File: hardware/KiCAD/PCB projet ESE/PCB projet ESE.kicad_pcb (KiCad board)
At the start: 4 copper layers, 57 x 54 mm, 95 parts, among them J1 Conn_01x06, J10 Conn_01x06, J11 Conn_01x06, J12 Conn_01x06, J13 Conn_01x06, J14 Conn_01x06, J15 Conn_01x06, J16 Conn_01x03, J2 Conn_01x04, J26 USB_C_Receptacle_USB2.0_16P, J3 Conn_01x06, J4 Conn_01x06, J5 Conn_01x04, J6 Conn_01x02, J7 Conn_ST_STDC14, J8 Conn_01x06, J9 Conn_01x06, SW1 SW_SPST, SW2 472121010111, U1 ZXBM5210-SP, U2 ZXBM5210-SP, U3 STM32G474RETx, U4 ADXL343, U5 USBLC6-2SC6

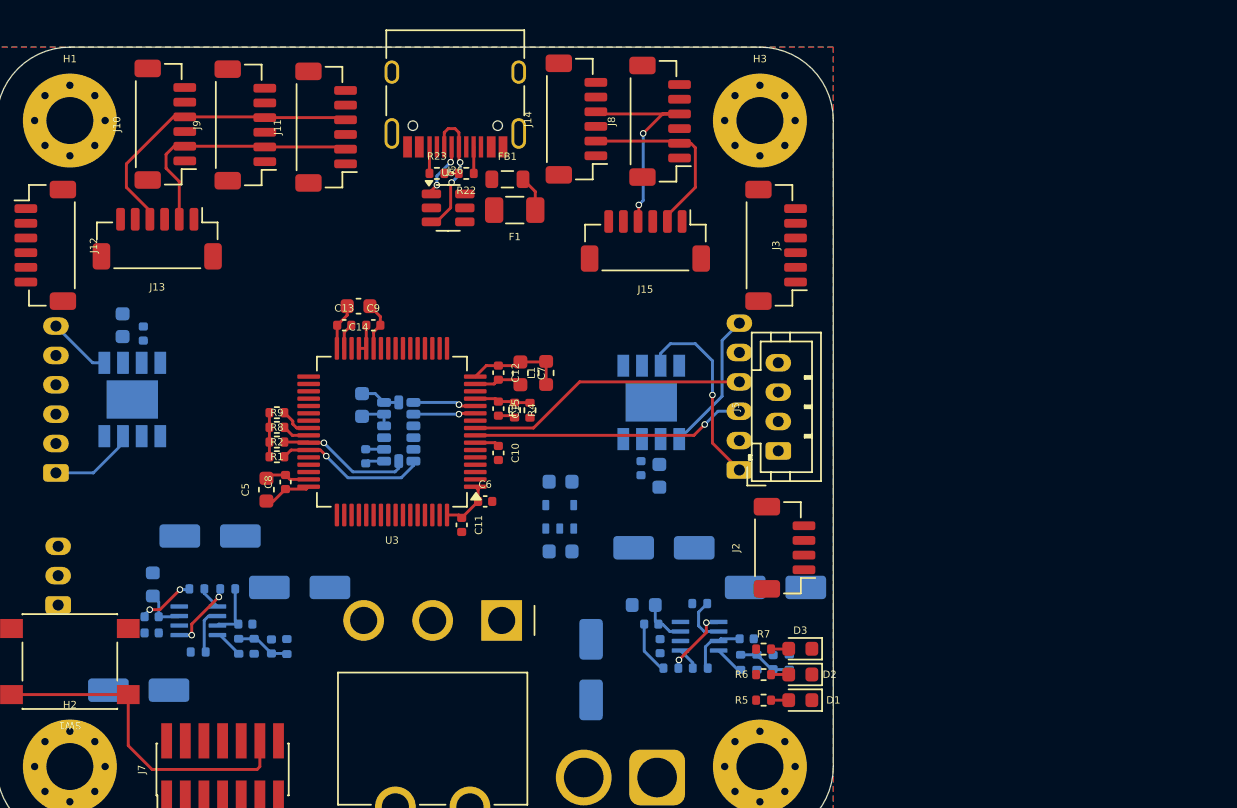
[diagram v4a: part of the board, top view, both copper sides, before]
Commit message: replace usb c by jst xh
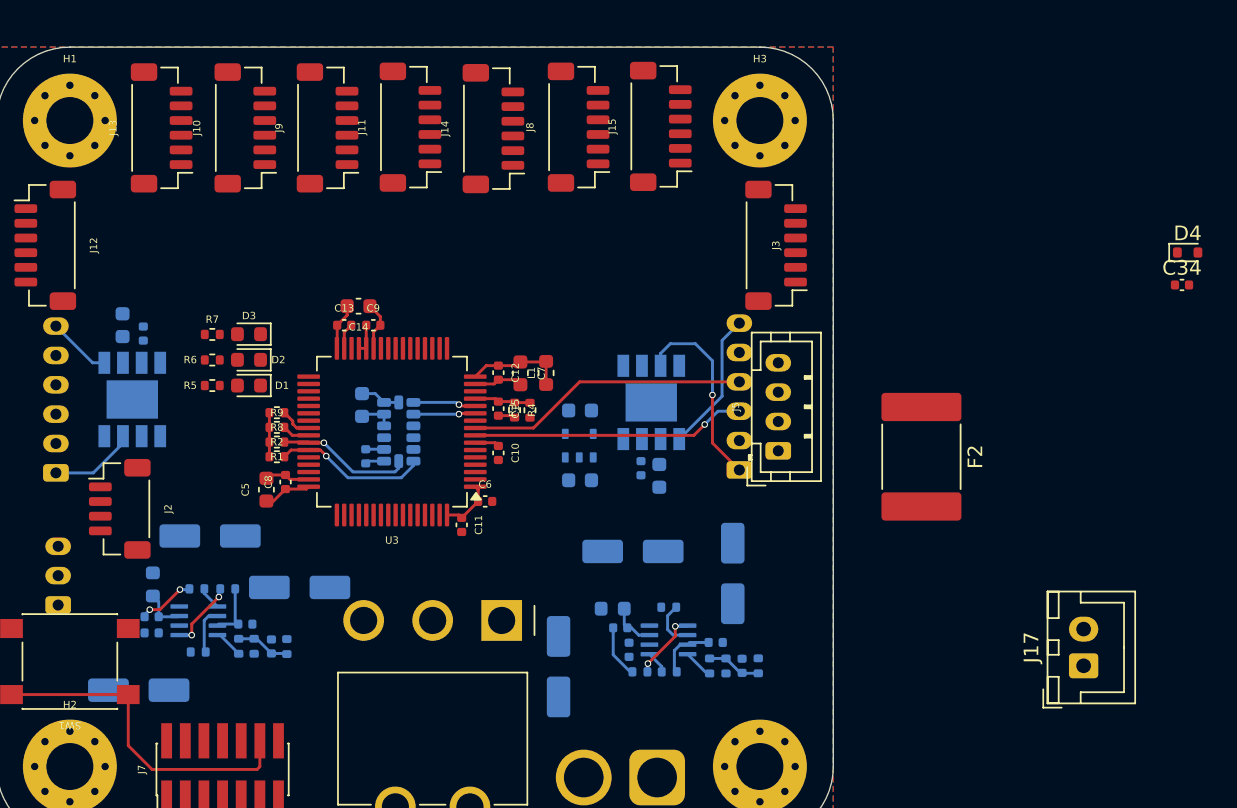
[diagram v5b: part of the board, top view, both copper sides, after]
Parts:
- removed F1: 250mA, Fuse:Fuse_1206_3216Metric
- removed FB1: 600 @ 100MHz, Inductor_SMD:L_0805_2012Metric
- removed J26: USB_C_Receptacle_USB2.0_16P, Connector_USB:USB_C_Receptacle_HRO_TYPE-C-31-M-12
- removed R22, R23: 5k1, Resistor_SMD:R_0402_1005Metric
- removed U5: USBLC6-2SC6, Package_TO_SOT_SMD:SOT-23-6
- added C34: 100n, Capacitor_SMD:C_0402_1005Metric, F.Cu at (159.8, 62.2)
- added D4: D_TVS_Small, Diode_SMD:D_SOD-523, F.Cu at (160.1, 60.0)
- added F2: 3.3A, Fuse:Fuse_2920_7451Metric, F.Cu at (142.0, 73.9)
- added J17: Conn_01x02, Connector_JST:JST_XH_B2B-XH-A_1x02_P2.50mm_Vertical, F.Cu at (153.1, 88.1)
- moved J2 45.4 mm to (87.4, 77.5), turned to -90 degrees
- moved D1 43.2 mm to (96.2, 69.0)
- moved D2 43.2 mm to (96.2, 67.3)
- moved D3 43.2 mm to (96.2, 65.5)
- moved R5 43.2 mm to (93.7, 69.0)
- moved R7 43.2 mm to (93.7, 65.6)
- moved R6 43.2 mm to (93.7, 67.3)
- moved J15 7.87 mm to (124.2, 51.4), turned to 90 degrees
- moved J13 7.56 mm to (90.2, 51.5), turned to 90 degrees
- moved J11 5.75 mm to (107.2, 51.5)
- moved J14 5.69 mm to (112.8, 51.5)
- moved J9 5.60 mm to (101.5, 51.5)
- moved J8 5.56 mm to (118.7, 51.5)
- moved J10 5.46 mm to (96.0, 51.5)
- moved BUxxSD1 5.03 mm to (118.7, 73.1)
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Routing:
- net SDA TOF: track 37.6 -> 1.88 mm, vias 2 -> 0
- net SCL TOF: track 32.3 -> 2.20 mm
- net D+: track 9.33 -> 0.00 mm, vias 2 -> 0
- net D-: track 3.77 -> 0.00 mm, vias 2 -> 0
- net Net-(F1-Pad1): track 2.45 -> 0.00 mm
- net Net-(J26-CC2): track 1.81 -> 0.00 mm
- net Net-(J26-CC1): track 1.81 -> 0.00 mm
- net Net-(D3-A): track 1.21 -> 0.00 mm
- net Net-(D2-A): track 1.21 -> 0.00 mm
- net Net-(D1-A): track 1.20 -> 0.00 mm
- net GND: track 17.3 -> 16.3 mm

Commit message: v1 PCB
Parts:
- removed C29, C30, C31: 22u, Capacitor_SMD:C_Elec_5x5.4
- removed C32, C33: 1u, Capacitor_SMD:C_0603_1608Metric
- removed C34: 100n, Capacitor_SMD:C_0402_1005Metric
- removed F2: 3.3A, Fuse:Fuse_2920_7451Metric
- removed J16: Conn_01x03, Connector_JST:JST_PH_B3B-PH-K_1x03_P2.00mm_Vertical
- removed J17: Conn_01x02, Connector_JST:JST_XH_B2B-XH-A_1x02_P2.50mm_Vertical
- removed L3: 4.7u, Inductor_SMD:L_0603_1608Metric
- removed MP2: ~, Régu:TSOT23-8
- removed R16, R17: 16k, Resistor_SMD:R_0402_1005Metric
- removed R18, R19: 7.68k, Resistor_SMD:R_0402_1005Metric
- removed R20, R21: 40.2k, Resistor_SMD:R_0402_1005Metric
- added ACCEL SCL: TestPoint, TestPoint:TestPoint_Pad_D1.0mm, B.Cu at (99.4, 79.9)
- added ACCEL SDA: TestPoint, TestPoint:TestPoint_Pad_D1.0mm, B.Cu at (102.6, 79.9)
- added F1: 3.3A, Fuse:Fuse_2920_7451Metric, B.Cu at (123.0, 81.0)
- added PWM FWD 1: TestPoint, TestPoint:TestPoint_Pad_D1.0mm, F.Cu at (119.0, 72.8)
- added PWM FWD 2: TestPoint, TestPoint:TestPoint_Pad_D1.0mm, F.Cu at (93.1, 72.6)
- added PWM REV 1: TestPoint, TestPoint:TestPoint_Pad_D1.0mm, F.Cu at (116.1, 66.9)
- added PWM REV 2: TestPoint, TestPoint:TestPoint_Pad_D1.0mm, F.Cu at (89.9, 82.4)
- C13: value 10n -> 100n
- C14: value 1u -> 100n; footprint Capacitor_SMD:C_0603_1608Metric -> Capacitor_SMD:C_0402_1005Metric
- C15: value 100n -> 10n
- C16: moved to F.Cu
- C17: value 0.1u -> 100n; moved to F.Cu
- C18, C28: value 22u -> 1u; footprint Capacitor_SMD:C_Elec_5x5.4 -> Capacitor_SMD:C_0603_1608Metric
- C19: value 22u -> 0.1u; footprint Capacitor_SMD:C_Elec_5x5.4 -> Capacitor_SMD:C_0402_1005Metric
- C20: value 0.1u -> 22u; footprint Capacitor_SMD:C_0402_1005Metric -> Capacitor_SMD:C_1206_3216Metric
- C24: value 0.1u -> 15p
- C25: value 0.1u -> 22u; footprint Capacitor_SMD:C_0402_1005Metric -> Capacitor_SMD:C_0603_1608Metric
- C26: value 15p -> 22u; footprint Capacitor_SMD:C_0402_1005Metric -> Capacitor_SMD:C_0603_1608Metric
- C27: value 15p -> 1u; footprint Capacitor_SMD:C_0402_1005Metric -> Capacitor_SMD:C_0603_1608Metric
- C5: value 4u7 -> 100n; footprint Capacitor_SMD:C_0603_1608Metric -> Capacitor_SMD:C_0402_1005Metric; moved to B.Cu
- C6: value 100n -> 4u7; footprint Capacitor_SMD:C_0402_1005Metric -> Capacitor_SMD:C_0603_1608Metric
- C7: value 1u -> 10u; footprint Capacitor_SMD:C_0603_1608Metric -> Capacitor_SMD:C_0402_1005Metric; moved to B.Cu
- C9: value 100n -> 1u; footprint Capacitor_SMD:C_0402_1005Metric -> Capacitor_SMD:C_0603_1608Metric
- D1: value LED -> D_TVS_Small; footprint LED_SMD:LED_0603_1608Metric -> Diode_SMD:D_SOD-523; moved to B.Cu
- D4: value D_TVS_Small -> LED; footprint Diode_SMD:D_SOD-523 -> LED_SMD:LED_0603_1608Metric
- H2, R1: moved to B.Cu
- J3: footprint Connector_JST:JST_SH_BM06B-SRSS-TB_1x06-1MP_P1.00mm_Vertical -> Connector_JST:JST_PH_B6B-PH-K_1x06_P2.00mm_Vertical; moved to B.Cu
- J4: value Conn_01x06 -> Conn_01x03; footprint Connector_JST:JST_PH_B6B-PH-K_1x06_P2.00mm_Vertical -> Connector_JST:JST_PH_B3B-PH-K_1x03_P2.00mm_Vertical; moved to F.Cu
- J5: value Conn_01x04 -> Conn_01x02; footprint Connector_JST:JST_PH_B4B-PH-K_1x04_P2.00mm_Vertical -> Connector_JST:JST_XH_B2B-XH-A_1x02_P2.50mm_Vertical
- J6: footprint Connector_AMASS:AMASS_XT30U-M_1x02_P5.0mm_Vertical -> Connector_JST:JST_SH_BM02B-SRSS-TB_1x02-1MP_P1.00mm_Vertical; moved to F.Cu
- J7: value Conn_ST_STDC14 -> Conn_01x04; footprint Connector_PinHeader_1.27mm:PinHeader_2x07_P1.27mm_Vertical_SMD -> Connector_JST:JST_PH_B4B-PH-K_1x04_P2.00mm_Vertical; moved to B.Cu
- J8: value Conn_01x06 -> Conn_01x02; footprint Connector_JST:JST_SH_BM06B-SRSS-TB_1x06-1MP_P1.00mm_Vertical -> Connector_AMASS:AMASS_XT30U-M_1x02_P5.0mm_Vertical; moved to B.Cu
- J9: value Conn_01x06 -> Conn_ST_STDC14; footprint Connector_JST:JST_SH_BM06B-SRSS-TB_1x06-1MP_P1.00mm_Vertical -> Connector_PinHeader_1.27mm:PinHeader_2x07_P1.27mm_Vertical_SMD
- R12: value 100k -> 20
- R13: value 100k -> 16k
- R14: value 20 -> 7.68k
- R15: value 20 -> 40.2k
- R2: value 1k -> 18k
- R3: value 18k -> 10k
- R4: value 10k -> 1k; moved to B.Cu
- moved D4 69.2 mm to (91.5, 68.6)
- moved H4 59.2 mm to (84.0, 59.0)
- moved J3 52.9 mm to (84.0, 81.5)
- moved J9 44.3 mm to (92.7, 94.9)
- moved H3 44.2 mm to (127.0, 95.0)
- moved J8 43.8 mm to (120.0, 95.2), turned to 180 degrees
- moved H1 43.7 mm to (127.0, 59.0)
- moved J7 38.0 mm to (89.8, 57.5), turned to -90 degrees
- moved D1 30.7 mm to (122.0, 85.6), turned to 90 degrees
- moved C5 28.8 mm to (124.5, 85.9), turned to -90 degrees
- moved L1 25.7 mm to (94.2, 81.1), turned to 180 degrees
- moved C25 24.9 mm to (114.0, 79.9)
- moved R11 24.4 mm to (117.1, 85.9), turned to -90 degrees
- moved R15 23.7 mm to (116.1, 79.7), turned to 90 degrees
- moved C23 23.3 mm to (112.8, 83.9), turned to -90 degrees
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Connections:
- C10 pad 1: NRST -> +3.3V
- C12 pad 1: +3.3V -> NRST
- C14 pad 1: GND -> +3.3V
- C14 pad 2: +3.3V -> GND
- C15 pad 1: ADC1_IN2 -> +3.3V
- C17 pad 1: +3.3V -> ADC1_IN2
- C18 pad 2: +7.4V -> +3.3V
- C19 pad 1: GND -> +3.3V
- C19 pad 2: +7.4V -> GND
- C20 pad 1: Net-(MP1-VCC) -> GND
- C20 pad 2: GND -> +7.4V
- C21 pad 1: Net-(MP2-VCC) -> Net-(MP1-VCC)
- C23 pad 1: GND -> Net-(C23-Pad1)
- C23 pad 2: +7.4V -> Net-(MP1-SW)
- C24 pad 2: Net-(MP1-SW) -> +5V
- C25 pad 1: Net-(C25-Pad1) -> GND
- C25 pad 2: Net-(MP2-SW) -> +5V
- C26 pad 1: Net-(C26-Pad1) -> GND
- C27 pad 1: Net-(C27-Pad1) -> +5V
- C27 pad 2: +5V -> GND
- C28 pad 1: GND -> +3.3V
- C28 pad 2: +5V -> GND
- C5 pad 1: +3.3V -> Net-(D1-A2)
- C7 pad 1: +3.3V -> Net-(D1-A2)
- D1 pad 2: Net-(D1-A) -> Net-(D1-A2)
- D4 pad 2: Net-(D4-A2) -> Net-(D4-A)
- J10 pad 1: INT_7 -> +3.3V
- J10 pad 2: SCL TOF -> GND
- J10 pad 3: XSHUT_7 -> SCL TOF
- J10 pad 5: +3.3V -> INT_1
- J10 pad 6: GND -> XSHUT_1
- J11 pad 1: INT_2 -> +3.3V
- J11 pad 2: SCL TOF -> GND
- J11 pad 3: XSHUT_2 -> SCL TOF
- J11 pad 5: +3.3V -> INT_4
- J11 pad 6: GND -> XSHUT_4
- J12 pad 1: INT_5 -> +3.3V
- J12 pad 2: SCL TOF -> GND
- J12 pad 3: XSHUT_5 -> SCL TOF
- J12 pad 5: +3.3V -> INT_2
- J12 pad 6: GND -> XSHUT_2
- J13 pad 1: INT_8 -> +3.3V
- J13 pad 2: SCL TOF -> GND
- J13 pad 3: XSHUT_8 -> SCL TOF
- J13 pad 5: +3.3V -> INT_5
- J13 pad 6: GND -> XSHUT_5
- J14 pad 1: INT_3 -> +3.3V
- J14 pad 2: SCL TOF -> GND
- J14 pad 3: XSHUT_3 -> SCL TOF
- J14 pad 5: +3.3V -> INT_3
- J14 pad 6: GND -> XSHUT_3
- J15 pad 1: INT_6 -> +3.3V
- J15 pad 2: SCL TOF -> GND
- J15 pad 3: XSHUT_6 -> SCL TOF
- J15 pad 5: +3.3V -> INT_6
- J15 pad 6: GND -> XSHUT_6
- J3 pad 1: unconnected-(J3-Pin_1-Pad1) -> Moteur - 2
- J3 pad 2: +5V -> GND
- J3 pad 3: GND -> Encodeur_A_Phase_2
- J3 pad 4: UART_HC05_RX -> Encodeur_B_Phase_2
- J3 pad 5: UART_HC05_TX -> +3.3V
- J3 pad 6: unconnected-(J3-Pin_6-Pad6) -> Moteur + 2
- J4 pad 1: Moteur - 2 -> GND
- J4 pad 2: GND -> PWM_LED1
- J4 pad 3: Encodeur_A_Phase_2 -> +5V
- J5 pad 1: +3.3V -> GND
- J5 pad 2: GND -> Net-(D1-A2)
- J6 pad 1: GND -> UART_Pi_Zero_TX
- J6 pad 2: Net-(J6-Pin_2) -> UART_PIi_Zero_RX
- J7 pad 1: unconnected-(J7-NC-Pad1) -> +3.3V
- J7 pad 2: unconnected-(J7-NC-Pad2) -> GND
- J7 pad 3: +3.3V -> Lidar Output 
- J7 pad 4: SWDIO -> +5V
- J8 pad 1: INT_1 -> GND
- J8 pad 2: SCL TOF -> Net-(J8-Pin_2)
- J9 pad 1: INT_4 -> unconnected-(J9-NC-Pad1)
- J9 pad 2: SCL TOF -> unconnected-(J9-NC-Pad2)
- J9 pad 3: XSHUT_4 -> +3.3V
- J9 pad 4: SDA TOF -> SWDIO
- J9 pad 5: +3.3V -> GND
- J9 pad 6: GND -> SWCLK
- R11 pad 1: +7.4V -> Net-(MP1-VCC)
- R11 pad 2: Net-(MP2-EN/SYNC) -> PG_51
- R12 pad 1: Net-(MP1-VCC) -> Net-(MP1-BST)
- R12 pad 2: PG_51 -> Net-(C23-Pad1)
- R13 pad 1: Net-(MP2-VCC) -> Net-(C24-Pad1)
- R13 pad 2: PG_52 -> Net-(MP1-FB)
- R14 pad 1: Net-(MP1-BST) -> Net-(C24-Pad1)
- R14 pad 2: Net-(C24-Pad1) -> GND
- R15 pad 1: Net-(MP2-BST) -> Net-(C24-Pad1)
- R15 pad 2: Net-(C25-Pad1) -> +5V
- R2 pad 1: +3.3V -> +7.4V
- R2 pad 2: Accel SCL -> ADC1_IN2
- R3 pad 1: +7.4V -> ADC1_IN2
- R3 pad 2: ADC1_IN2 -> GND
- R4 pad 1: ADC1_IN2 -> +3.3V
- R4 pad 2: GND -> Accel SCL
- R5 pad 2: Net-(D1-A) -> Net-(D2-A)
- R6 pad 2: Net-(D2-A) -> Net-(D3-A)
- R7 pad 2: Net-(D3-A) -> Net-(D4-A)
- SW2 pad 2: Net-(J6-Pin_2) -> Net-(J8-Pin_2)
- U3 pad 14: UART_HC05_TX -> UART_Pi_Zero_TX
- U3 pad 17: UART_HC05_RX -> UART_PIi_Zero_RX
- U3 pad 3: Lidar Output  -> unconnected-(U3-PC14-Pad3)
- U3 pad 33: XSHUT_7 -> XSHUT_5
- U3 pad 34: INT_7 -> INT_5
- U3 pad 35: INT_8 -> Lidar Output 
- U3 pad 36: XSHUT_8 -> unconnected-(U3-PB14-Pad36)
- U3 pad 37: INT_5 -> unconnected-(U3-PB15-Pad37)
- U3 pad 44: XSHUT_5 -> unconnected-(U3-PA10-Pad44)
- U3 pad 45: USB_DM -> unconnected-(U3-PA11-Pad45)
- U3 pad 46: USB_DP -> unconnected-(U3-PA12-Pad46)
- U3 pad 51: PG_52 -> unconnected-(U3-PA15-Pad51)
- U3 pad 8: Encodeur_A_Phase_1 -> Encodeur_B_Phase_1
- U3 pad 9: Encodeur_B_Phase_1 -> Encodeur_A_Phase_1
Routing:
- net SDA TOF: track 1.88 -> 56.0 mm, vias 0 -> 7
- net SCL TOF: track 2.20 -> 53.0 mm, vias 0 -> 8
- net GND: track 16.3 -> 61.4 mm, vias 0 -> 100
- net UART_PIi_Zero_RX: track 0.00 -> 27.4 mm, vias 0 -> 2
- net UART_mp3_RX: track 0.00 -> 24.8 mm, vias 0 -> 2
- net XSHUT_6: track 0.00 -> 24.7 mm
- net UART_mp3_TX: track 0.00 -> 24.4 mm, vias 0 -> 2
- net PWM REV 1: track 0.00 -> 23.8 mm, vias 0 -> 2
- net INT_6: track 0.00 -> 23.4 mm
- net PWM_LED1: track 0.00 -> 22.9 mm, vias 0 -> 1
- net PWM FWD 1: track 0.00 -> 22.7 mm, vias 0 -> 2
- net UART_Pi_Zero_TX: track 0.00 -> 21.3 mm, vias 0 -> 2
- net XSHUT_1: track 0.00 -> 19.9 mm
- net PWM FWD 2: track 0.00 -> 19.6 mm, vias 0 -> 2
- net INT_1: track 0.00 -> 18.8 mm
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- added copper zone on In2.Cu, net +3.3V
- added copper zone on In2.Cu, net +5V
- added copper zone on In2.Cu, net +7.4V
- removed copper zone on In2.Cu, net Net-(J6-Pin_2)
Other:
- board size 57 x 54 mm -> 53 x 46 mm
- board text added: "+3V +5V +7.4V"
- board text added: "Alim Pi Zero 2W"
- board text added: "ESE ROBOT CHAT"
- board text added: "LED"
- board text added: "MP3"
- board text added: "Moteur"
- board text added: "TOF"
- board text added: "UART Pi Zero 2W"
- board text added: "V. FERNANDES"

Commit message: maj pcb and pinout
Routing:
- net Net-(J8-Pin_2): track 14.6 -> 16.0 mm
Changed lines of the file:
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@@
 		(tags "connector JST PH side entry")
 		(property "Reference" "J4"
-			(at 2.1 4.05 -270)
+			(at 2.1 4.05 90)
 			(layer "F.SilkS")
 			(effects
@@
 		(tags "LQFP QFP")
 		(property "Reference" "U3"
-			(at 0 -7.4 0)
+			(at 5.775 -5.15 0)
 			(layer "F.SilkS")
 			(effects
@@
 		(tags "THT")
 		(property "Reference" "SW2"
-			(at 4.75975 -27.74975 180)
+			(at -3.135125 -13.975 0)
 			(unlocked yes)
 			(layer "F.SilkS")
@@
 		)
 	)
+	(gr_text "ESE ROBOT CHAT"
+		(at 107.95 94.75 0)
+		(layer "B.SilkS" knockout)
+		(effects
+			(font
+				(size 1 1)
+				(thickness 0.25)
+				(bold yes)
+			)
+			(justify left bottom mirror)
+		)
+	)
 	(gr_text "V. FERNANDES"
-		(at 108.05 93.925 0)
+		(at 107.8 93.2 0)
 		(layer "B.SilkS" knockout)
 		(effects
 			(font
-				(size 0.5 0.5)
-				(thickness 0.125)
+				(size 1 1)
+				(thickness 0.25)
 				(bold yes)
 			)
@@
 		)
 	)
-	(gr_text "ESE ROBOT CHAT"
-		(at 108.125 94.7 0)
-		(layer "B.SilkS" knockout)
-		(effects
-			(font
-				(size 0.5 0.5)
-				(thickness 0.125)
-				(bold yes)
-			)
-			(justify left bottom mirror)
-		)
-	)
 	(gr_text "Moteur"
 		(at 130.875 69.45 90)
@@
 	)
 	(via
-		(at 108.175 90.2)
+		(at 108.7 94.025)
 		(size 0.45)
 		(drill 0.3)
@@
 	)
 	(via
-		(at 103.05 91.725)
+		(at 105.15 90.9)
 		(size 0.45)
 		(drill 0.3)
@@
 	)
 	(via
-		(at 104.7 87)
+		(at 102.475 87.025)
 		(size 0.45)
 		(drill 0.3)
@@
 	(segment
 		(start 104.740125 84.85)
+		(end 104.740125 87.215125)
+		(width 1.5)
+		(layer "B.Cu")
+		(net 76)
+	)
+	(segment
+		(start 112.634875 95.109875)
 		(end 115 95.109875)
-		(width 0.2)
+		(width 1.5)
 		(layer "B.Cu")
 		(net 76)
@@
 		(layer "B.Cu")
 		(net 76)
+	)
+	(segment
+		(start 104.740125 87.215125)
+		(end 112.634875 95.109875)
+		(width 1.5)
+		(layer "B.Cu")
+		(net 76)

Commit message: update
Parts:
- removed C5: 100n, Capacitor_SMD:C_0402_1005Metric
- removed C7: 10u, Capacitor_SMD:C_0402_1005Metric
- removed D1: D_TVS_Small, Diode_SMD:D_SOD-523
- removed F1: 3.3A, Fuse:Fuse_2920_7451Metric
- removed J5: Conn_01x02, Connector_JST:JST_XH_B2B-XH-A_1x02_P2.50mm_Vertical
- removed J6: Conn_01x02, Connector_JST:JST_SH_BM02B-SRSS-TB_1x02-1MP_P1.00mm_Vertical
- added C29: 100n, Capacitor_SMD:C_0402_1005Metric, B.Cu at (125.3, 86.1)
- added C30: 10u, Capacitor_SMD:C_0603_1608Metric, B.Cu at (124.0, 86.3)
- added D5: D_TVS_Small, Diode_SMD:D_SOD-523, B.Cu at (122.5, 86.2)
- added F2: 3.3A, Fuse:Fuse_2920_7451Metric, B.Cu at (121.6, 80.1)
- added J16: Conn_01x04, Connector_JST:JST_PH_B4B-PH-K_1x04_P2.00mm_Vertical, F.Cu at (126.8, 87.6)
- J1, J3: footprint Connector_JST:JST_PH_B6B-PH-K_1x06_P2.00mm_Vertical -> Connector_JST:JST_PH_S6B-PH-K_1x06_P2.00mm_Horizontal
- moved L2 1.02 mm to (117.9, 88.6), turned to -90 degrees
- moved PWM FWD 1 0.87 mm to (119.0, 71.9)
- moved C2 0.57 mm to (89.9, 80.5)
- moved ACCEL SCL 0.41 mm to (99.1, 79.7)
- moved PWM FWD 2 0.22 mm to (93.3, 72.5)
- moved PWM REV 2 0.14 mm to (89.8, 82.5)
- moved ACCEL SDA 0.10 mm to (102.6, 79.8)
- moved PWM REV 1 0.10 mm to (116.0, 66.9)
- moved C16 0.08 mm to (108.2, 81.3)
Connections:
- J10 pad MP: (no net) -> GND
- J11 pad MP: (no net) -> GND
- J12 pad MP: (no net) -> GND
- J13 pad MP: (no net) -> GND
- J14 pad MP: (no net) -> GND
- J15 pad MP: (no net) -> GND
- J2 pad MP: (no net) -> GND
- U3 pad 17: UART_PIi_Zero_RX -> UART_Pi_Zero_RX
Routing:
- net UART_Pi_Zero_RX: track 0.00 -> 30.1 mm, vias 0 -> 2
- net UART_PIi_Zero_RX: track 27.4 -> 0.00 mm, vias 2 -> 0
- net GND: track 61.4 -> 85.9 mm, vias 100 -> 116
- net Net-(D1-A2): track 10.6 -> 0.00 mm
- net Net-(D5-A2): track 0.00 -> 6.68 mm
- net UART_Pi_Zero_TX: track 21.3 -> 25.0 mm
- net Net-(MP1-SW): track 7.53 -> 9.43 mm, vias 2 -> 5
- net PWM FWD 1: track 22.7 -> 21.9 mm
- net +5V: track 15.6 -> 16.4 mm, vias 11 -> 10
- net Moteur - 1: track 5.30 -> 5.88 mm
- added copper zone on B.Cu, net Net-(MP1-SW)
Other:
- board text added: "Pi Zero 2W"
- board text removed: "Alim Pi Zero 2W"
- board text removed: "UART Pi Zero 2W"
